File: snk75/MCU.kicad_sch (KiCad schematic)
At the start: 2 parts, among them U2 STM32F072C8Tx

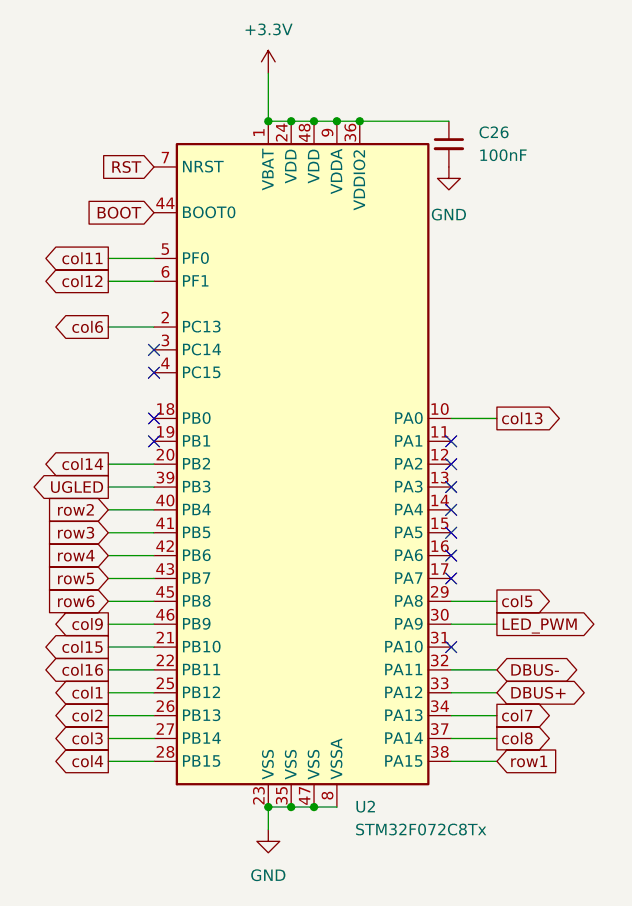
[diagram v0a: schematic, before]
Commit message: added components on board and began routing
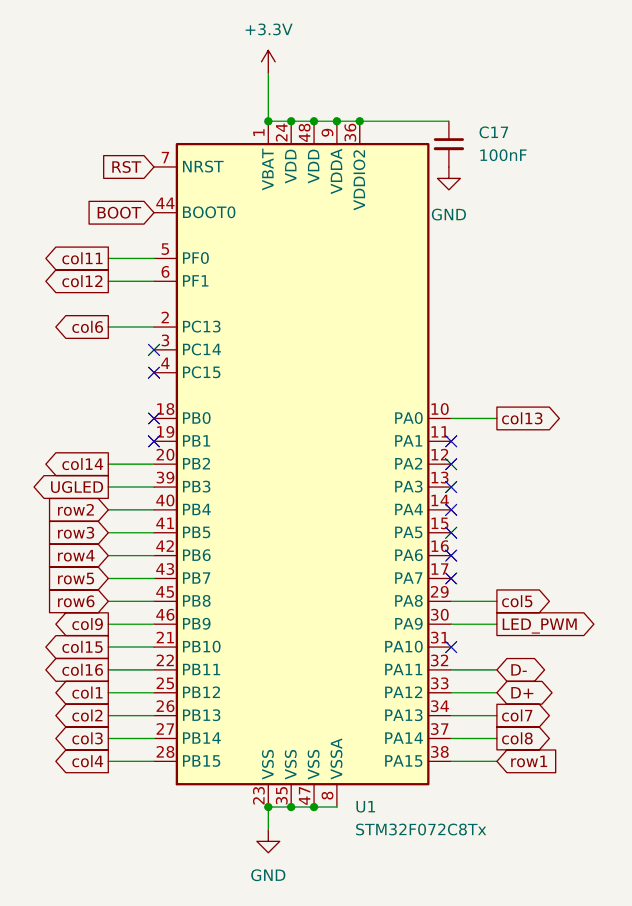
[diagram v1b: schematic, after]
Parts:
- renumbered C26 to C17, U2 to U1
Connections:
- net DBUS+ renamed D+
- net DBUS- renamed D-
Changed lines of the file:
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@@
     )
   )
-  (global_label "DBUS-" (shape bidirectional) (at 162.56 119.38 0) (fields_autoplaced)
-    (effects (font (size 1.27 1.27)) (justify left))
-    (property "Intersheet References" "${INTERSHEET_REFS}" (id 0) (at 171.6255 119.3006 0)
+  (global_label "D-" (shape bidirectional) (at 162.56 119.38 0) (fields_autoplaced)
+    (effects (font (size 1.27 1.27)) (justify left))
+    (property "Intersheet References" "${INTERSHEET_REFS}" (id 0) (at 167.8155 119.3006 0)
       (effects (font (size 1.27 1.27)) (justify left) hide)
     )
@@
     )
   )
-  (global_label "DBUS+" (shape bidirectional) (at 162.56 121.92 0) (fields_autoplaced)
-    (effects (font (size 1.27 1.27)) (justify left))
-    (property "Intersheet References" "${INTERSHEET_REFS}" (id 0) (at 171.6255 121.8406 0)
+  (global_label "D+" (shape bidirectional) (at 162.56 121.92 0) (fields_autoplaced)
+    (effects (font (size 1.27 1.27)) (justify left))
+    (property "Intersheet References" "${INTERSHEET_REFS}" (id 0) (at 167.8155 121.8406 0)
       (effects (font (size 1.27 1.27)) (justify left) hide)
     )
@@
   (symbol (lib_id "Device:C_Small") (at 157.226 60.96 0) (unit 1)
     (in_bom yes) (on_board yes) (fields_autoplaced)
-    (property "Reference" "C26" (id 0) (at 160.528 59.6962 0)
+    (property "Reference" "C17" (id 0) (at 160.528 59.6962 0)
       (effects (font (size 1.27 1.27)) (justify left))
     )
@@
   (symbol (lib_id "MCU_ST_STM32F0:STM32F072C8Tx") (at 142.24 96.52 0) (unit 1)
     (in_bom yes) (on_board yes) (fields_autoplaced)
-    (property "Reference" "U2" (id 0) (at 146.7994 134.62 0)
+    (property "Reference" "U1" (id 0) (at 146.7994 134.62 0)
       (effects (font (size 1.27 1.27)) (justify left))
     )
@@
   (symbol (lib_id "power:+3.3V") (at 137.16 53.086 0) (unit 1)
     (in_bom yes) (on_board yes) (fields_autoplaced)
-    (property "Reference" "#PWR045" (id 0) (at 137.16 56.896 0)
+    (property "Reference" "#PWR033" (id 0) (at 137.16 56.896 0)
       (effects (font (size 1.27 1.27)) hide)
     )
@@
   (symbol (lib_id "power:GND") (at 157.226 63.5 0) (unit 1)
     (in_bom yes) (on_board yes) (fields_autoplaced)
-    (property "Reference" "#PWR047" (id 0) (at 157.226 69.85 0)
+    (property "Reference" "#PWR035" (id 0) (at 157.226 69.85 0)
       (effects (font (size 1.27 1.27)) hide)
     )
@@
   (symbol (lib_id "power:GND") (at 137.16 137.16 0) (unit 1)
     (in_bom yes) (on_board yes) (fields_autoplaced)
-    (property "Reference" "#PWR046" (id 0) (at 137.16 143.51 0)
-      (effects (font (size 1.27 1.27)) hide)
-    )
+    (property "Reference" "#PWR034" (id 0) (at 137.16 143.51 0)
+      (effects (font (size 1.27 1.27)) hide)
+    )

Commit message: Re routed paths for cols and rows
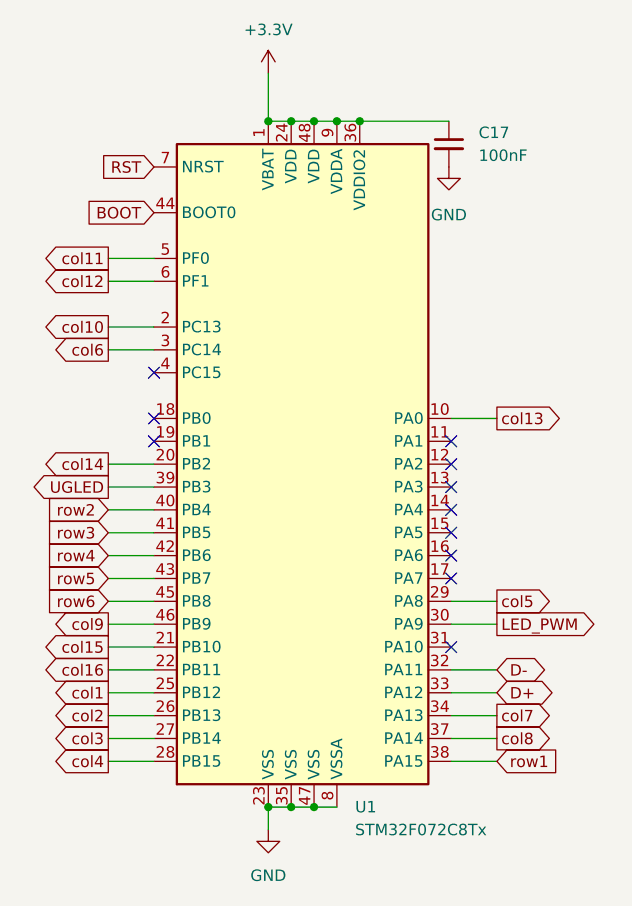
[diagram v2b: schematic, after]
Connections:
- net col6: now also U1.3 (PC14); no longer U1.2 (PC13)
- new net col10: U1.2 (PC13)
- no-connect marks 12 -> 11
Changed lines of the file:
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@@
   (no_connect (at 157.48 101.6))
   (no_connect (at 124.46 86.36))
-  (no_connect (at 124.46 83.82))
   (no_connect (at 157.48 96.52))
   (no_connect (at 157.48 99.06))
@@
     (stroke (width 0) (type default) (color 0 0 0 0))
   )
+  (wire (pts (xy 119.38 83.82) (xy 124.46 83.82))
+    (stroke (width 0) (type default) (color 0 0 0 0))
+  )
   (wire (pts (xy 139.7 58.42) (xy 142.24 58.42))
     (stroke (width 0) (type default) (color 0 0 0 0))
@@
     )
   )
+  (global_label "col6" (shape output) (at 119.38 83.82 180) (fields_autoplaced)
+    (effects (font (size 1.27 1.27)) (justify right))
+    (property "Intersheet References" "${INTERSHEET_REFS}" (id 0) (at 112.8545 83.7406 0)
+      (effects (font (size 1.27 1.27)) (justify right) hide)
+    )
+  )
   (global_label "RST" (shape input) (at 124.46 63.5 180) (fields_autoplaced)
     (effects (font (size 1.27 1.27)) (justify right))
@@
     )
   )
-  (global_label "col6" (shape output) (at 119.38 81.28 180) (fields_autoplaced)
-    (effects (font (size 1.27 1.27)) (justify right))
-    (property "Intersheet References" "${INTERSHEET_REFS}" (id 0) (at 112.8545 81.2006 0)
-      (effects (font (size 1.27 1.27)) (justify right) hide)
-    )
+  (global_label "col10" (shape output) (at 119.38 81.28 180) (fields_autoplaced)
+    (effects (font (size 1.27 1.27)) (justify right))
+    (property "Intersheet References" "${INTERSHEET_REFS}" (id 0) (at 111.645 81.2006 0)
+      (effects (font (size 1.27 1.27)) (justify right) hide)
+    )

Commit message: Nearly make all paths
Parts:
- C17: JLCPCB BOM (none) -> 1; LCSC (none) -> C1525; LCSC Part (none) -> C1525; LCSC Part Number (none) -> C1525
- U1: JLCPCB BOM (none) -> 1; LCSC (none) -> C80488; LCSC Part (none) -> C80488; LCSC Part Number (none) -> C80488
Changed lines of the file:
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@@
+      (effects (font (size 1.27 1.27)) hide)
+    )
+    (property "LCSC" "C1525" (id 4) (at 157.226 60.96 0)
+      (effects (font (size 1.27 1.27)) hide)
+    )
+    (property "LCSC Part" "C1525" (id 5) (at 157.226 60.96 0)
+      (effects (font (size 1.27 1.27)) hide)
+    )
+    (property "LCSC Part Number" "C1525" (id 6) (at 157.226 60.96 0)
+      (effects (font (size 1.27 1.27)) hide)
+    )
+    (property "JLCPCB BOM" "1" (id 7) (at 157.226 60.96 0)
       (effects (font (size 1.27 1.27)) hide)
     )
@@
       (effects (font (size 1.27 1.27)) hide)
     )
+    (property "LCSC Part" "C80488" (id 4) (at 142.24 96.52 0)
+      (effects (font (size 1.27 1.27)) hide)
+    )
+    (property "LCSC" "C80488" (id 5) (at 142.24 96.52 0)
+      (effects (font (size 1.27 1.27)) hide)
+    )
+    (property "LCSC Part Number" "C80488" (id 6) (at 142.24 96.52 0)
+      (effects (font (size 1.27 1.27)) hide)
+    )
+    (property "JLCPCB BOM" "1" (id 7) (at 142.24 96.52 0)
+      (effects (font (size 1.27 1.27)) hide)
+    )
